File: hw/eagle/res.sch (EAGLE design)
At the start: 63 parts, among them IC2 7805T, IC3 L272M, IC4 L272M, X5 22-23-2021

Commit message: +c
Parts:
- added C16: (no value), rcl:C-EU050-025X075
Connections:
- net +5V: now also C16.1, R4.A; no longer R4.E
- net GND: now also C16.2
- net N$2: now also R4.E; no longer R4.A
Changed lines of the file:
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@@
 <part name="GND35" library="supply1" deviceset="GND" device=""/>
 <part name="GND36" library="supply1" deviceset="GND" device=""/>
+<part name="C16" library="rcl" deviceset="C-EU" device="050-025X075"/>
+<part name="GND37" library="supply1" deviceset="GND" device=""/>
 </parts>
 <sheets>
@@
 <instance part="R2" gate="G$1" x="96.52" y="185.42" rot="R270"/>
 <instance part="R3" gate="G$1" x="152.4" y="177.8" rot="R180"/>
-<instance part="R4" gate="1" x="104.14" y="193.04" rot="MR270"/>
+<instance part="R4" gate="1" x="104.14" y="193.04" rot="R270"/>
 <instance part="R5" gate="G$1" x="144.78" y="200.66" rot="R270"/>
 <instance part="R6" gate="G$1" x="142.24" y="195.58" rot="R270"/>
@@
 <instance part="GND35" gate="1" x="391.16" y="111.76" rot="R90"/>
 <instance part="GND36" gate="1" x="391.16" y="109.22" rot="R90"/>
+<instance part="C16" gate="G$1" x="81.28" y="208.28"/>
+<instance part="GND37" gate="1" x="81.28" y="200.66"/>
 </instances>
 <busses>
@@
 <wire x1="124.46" y1="177.8" x2="121.92" y2="177.8" width="0.1524" layer="91"/>
 <junction x="124.46" y="177.8"/>
-<pinref part="R4" gate="1" pin="A"/>
+<pinref part="R4" gate="1" pin="E"/>
 <wire x1="109.22" y1="193.04" x2="124.46" y2="193.04" width="0.1524" layer="91"/>
 </segment>
@@
 <pinref part="LED2" gate="G$1" pin="C"/>
 <pinref part="GND36" gate="1" pin="GND"/>
+</segment>
+<segment>
+<pinref part="C16" gate="G$1" pin="2"/>
+<pinref part="GND37" gate="1" pin="GND"/>
 </segment>
 </net>
@@
 <segment>
 <pinref part="R2" gate="G$1" pin="1"/>
-<wire x1="96.52" y1="213.36" x2="96.52" y2="210.82" width="0.1524" layer="91"/>
 <wire x1="96.52" y1="210.82" x2="96.52" y2="193.04" width="0.1524" layer="91"/>
 <wire x1="96.52" y1="193.04" x2="96.52" y2="190.5" width="0.1524" layer="91"/>
@@
 <wire x1="142.24" y1="210.82" x2="129.54" y2="210.82" width="0.1524" layer="91"/>
 <wire x1="129.54" y1="210.82" x2="96.52" y2="210.82" width="0.1524" layer="91"/>
-<wire x1="96.52" y1="210.82" x2="73.66" y2="210.82" width="0.1524" layer="91"/>
+<wire x1="96.52" y1="210.82" x2="81.28" y2="210.82" width="0.1524" layer="91"/>
+<wire x1="81.28" y1="210.82" x2="73.66" y2="210.82" width="0.1524" layer="91"/>
 <wire x1="73.66" y1="210.82" x2="66.04" y2="210.82" width="0.1524" layer="91"/>
 <wire x1="96.52" y1="213.36" x2="96.52" y2="210.82" width="0.1524" layer="91"/>
@@
 <junction x="66.04" y="210.82"/>
 <junction x="129.54" y="210.82"/>
-<pinref part="R4" gate="1" pin="E"/>
 <wire x1="129.54" y1="175.26" x2="129.54" y2="210.82" width="0.1524" layer="91"/>
-<wire x1="96.52" y1="193.04" x2="99.06" y2="193.04" width="0.1524" layer="91"/>
 <pinref part="X1" gate="-" pin="3"/>
 <wire x1="160.02" y1="190.5" x2="152.4" y2="190.5" width="0.1524" layer="91"/>
@@
 <junction x="73.66" y="210.82"/>
 <junction x="96.52" y="210.82"/>
-<junction x="96.52" y="193.04"/>
 <junction x="152.4" y="220.98"/>
 <junction x="129.54" y="175.26"/>
-</segment>
-<segment>
+<pinref part="R4" gate="1" pin="A"/>
+<wire x1="96.52" y1="193.04" x2="99.06" y2="193.04" width="0.1524" layer="91"/>
+<pinref part="C16" gate="G$1" pin="1"/>
+<junction x="81.28" y="210.82"/>
+</segment>
+<segment>

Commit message: gnd
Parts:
- added C17: (no value), rcl:C-EU050-025X075
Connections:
- net GND: now also C17.2
- net N$36: now also C17.1
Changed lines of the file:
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@@
 <part name="C16" library="rcl" deviceset="C-EU" device="050-025X075"/>
 <part name="GND37" library="supply1" deviceset="GND" device=""/>
+<part name="C17" library="rcl" deviceset="C-EU" device="050-025X075"/>
+<part name="GND38" library="supply1" deviceset="GND" device=""/>
 </parts>
 <sheets>
@@
 <instance part="C16" gate="G$1" x="81.28" y="208.28"/>
 <instance part="GND37" gate="1" x="81.28" y="200.66"/>
+<instance part="C17" gate="G$1" x="373.38" y="162.56" rot="R90"/>
+<instance part="GND38" gate="1" x="381" y="162.56" rot="R90"/>
 </instances>
 <busses>
@@
 <pinref part="GND37" gate="1" pin="GND"/>
 </segment>
+<segment>
+<pinref part="C17" gate="G$1" pin="2"/>
+<pinref part="GND38" gate="1" pin="GND"/>
+</segment>
 </net>
 <net name="N$8" class="0">
@@
 <junction x="322.58" y="167.64"/>
 <junction x="340.36" y="162.56"/>
+<pinref part="C17" gate="G$1" pin="1"/>
+<junction x="370.84" y="162.56"/>
 </segment>
 </net>
@@
 <pinref part="C16" gate="G$1" pin="1"/>
 <junction x="81.28" y="210.82"/>
-</segment>
-<segment>
+<junction x="96.52" y="193.04"/>
+</segment>
+<segment>

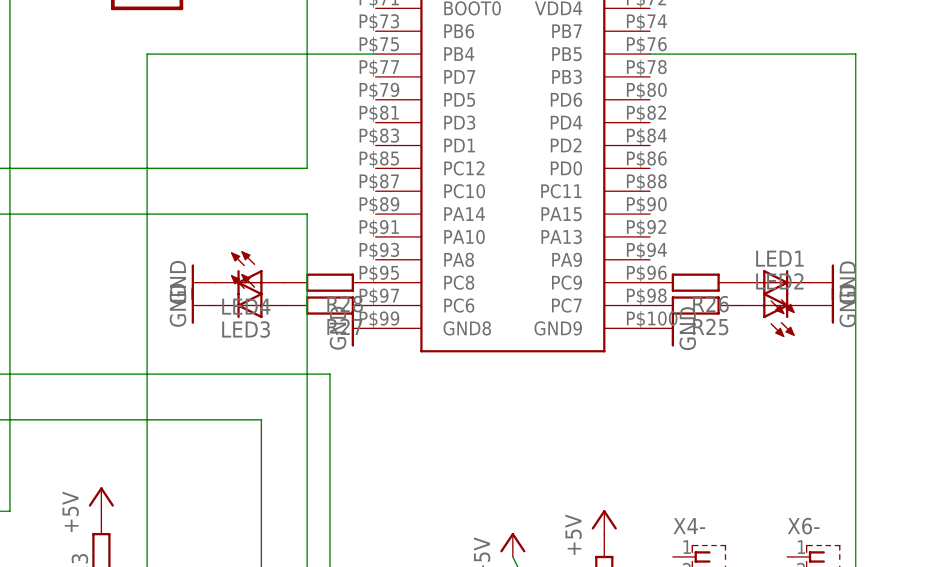
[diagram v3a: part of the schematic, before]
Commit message: led umgeklemmt
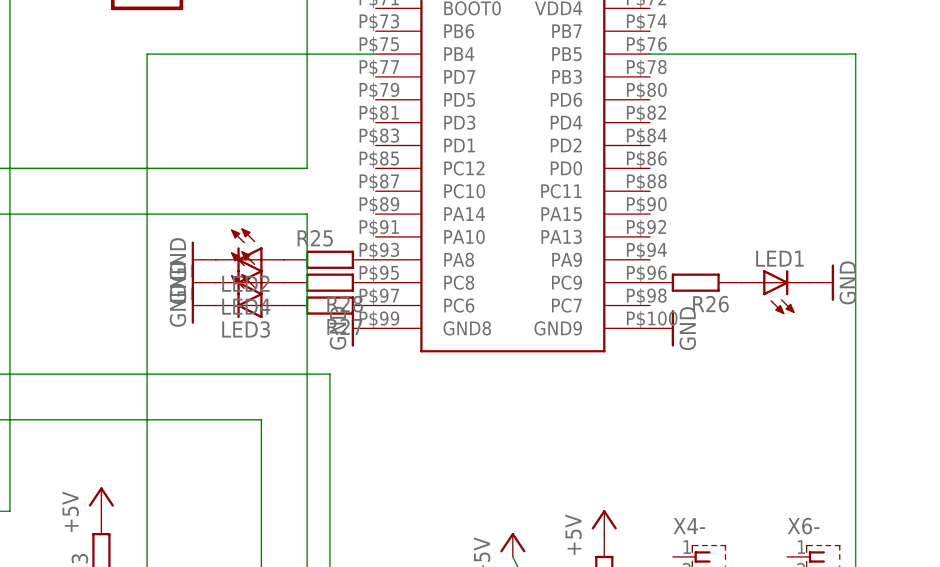
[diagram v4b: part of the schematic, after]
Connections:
- removed net N$46 (its old number): R25.2, U$1.PC7
- new net N$51: R25.2, U$1.PA8
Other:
- moved on the sheet: LED2, R25
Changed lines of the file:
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@@
 <instance part="X6" gate="SHIELD@3" x="395.224" y="64.77"/>
 <instance part="X6" gate="SHIELD@4" x="398.78" y="64.77"/>
-<instance part="R25" gate="G$1" x="375.92" y="109.22" rot="R180"/>
+<instance part="R25" gate="G$1" x="335.28" y="114.3"/>
 <instance part="R26" gate="G$1" x="375.92" y="111.76" rot="R180"/>
 <instance part="R27" gate="G$1" x="335.28" y="109.22" rot="R180"/>
 <instance part="R28" gate="G$1" x="335.28" y="111.76" rot="R180"/>
 <instance part="LED1" gate="G$1" x="383.54" y="111.76" rot="R90"/>
-<instance part="LED2" gate="G$1" x="383.54" y="109.22" rot="R90"/>
+<instance part="LED2" gate="G$1" x="327.66" y="114.3" rot="R270"/>
 <instance part="LED3" gate="G$1" x="327.66" y="109.22" rot="R270"/>
 <instance part="LED4" gate="G$1" x="327.66" y="111.76" rot="R270"/>
@@
 <instance part="GND34" gate="1" x="320.04" y="109.22" rot="R270"/>
 <instance part="GND35" gate="1" x="391.16" y="111.76" rot="R90"/>
-<instance part="GND36" gate="1" x="391.16" y="109.22" rot="R90"/>
+<instance part="GND36" gate="1" x="320.04" y="114.3" rot="R270"/>
 <instance part="C16" gate="G$1" x="81.28" y="208.28"/>
 <instance part="GND37" gate="1" x="81.28" y="200.66"/>
@@
 </segment>
 </net>
-<net name="N$46" class="0">
-<segment>
-<pinref part="U$1" gate="G$1" pin="PC7"/>
-<pinref part="R25" gate="G$1" pin="2"/>
-</segment>
-</net>
 <net name="N$47" class="0">
 <segment>
@@
 </segment>
 </net>
-<net name="N$51" class="0">
+<net name="N$52" class="0">
+<segment>
+<pinref part="R27" gate="G$1" pin="2"/>
+<pinref part="LED3" gate="G$1" pin="A"/>
+</segment>
+</net>
+<net name="N$53" class="0">
+<segment>
+<pinref part="R28" gate="G$1" pin="2"/>
+<pinref part="LED4" gate="G$1" pin="A"/>
+</segment>
+</net>
+<net name="N$46" class="0">
 <segment>
 <pinref part="R25" gate="G$1" pin="1"/>
@@
 </segment>
 </net>
-<net name="N$52" class="0">
-<segment>
-<pinref part="R27" gate="G$1" pin="2"/>
-<pinref part="LED3" gate="G$1" pin="A"/>
-</segment>
-</net>
-<net name="N$53" class="0">
-<segment>
-<pinref part="R28" gate="G$1" pin="2"/>
-<pinref part="LED4" gate="G$1" pin="A"/>
-</segment>
-</net>
+<net name="N$51" class="0">
+<segment>
+<pinref part="U$1" gate="G$1" pin="PA8"/>
+<pinref part="R25" gate="G$1" pin="2"/>
+</segment>
+</net>

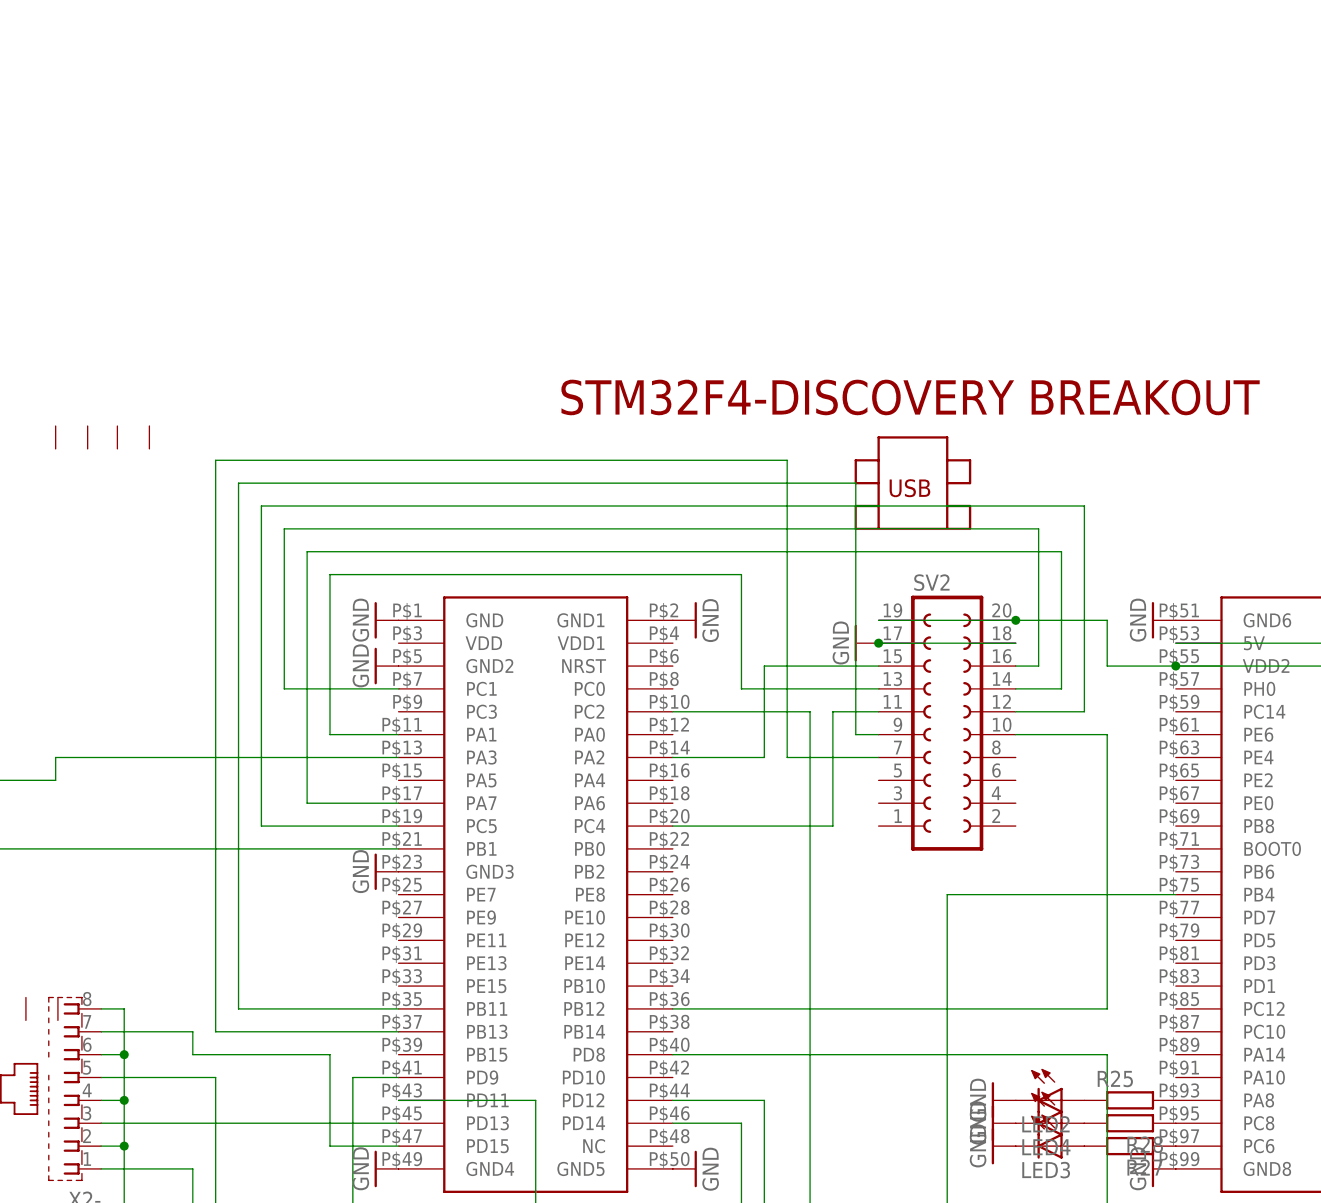
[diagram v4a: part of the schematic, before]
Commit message: schaltplan aufgeräumt
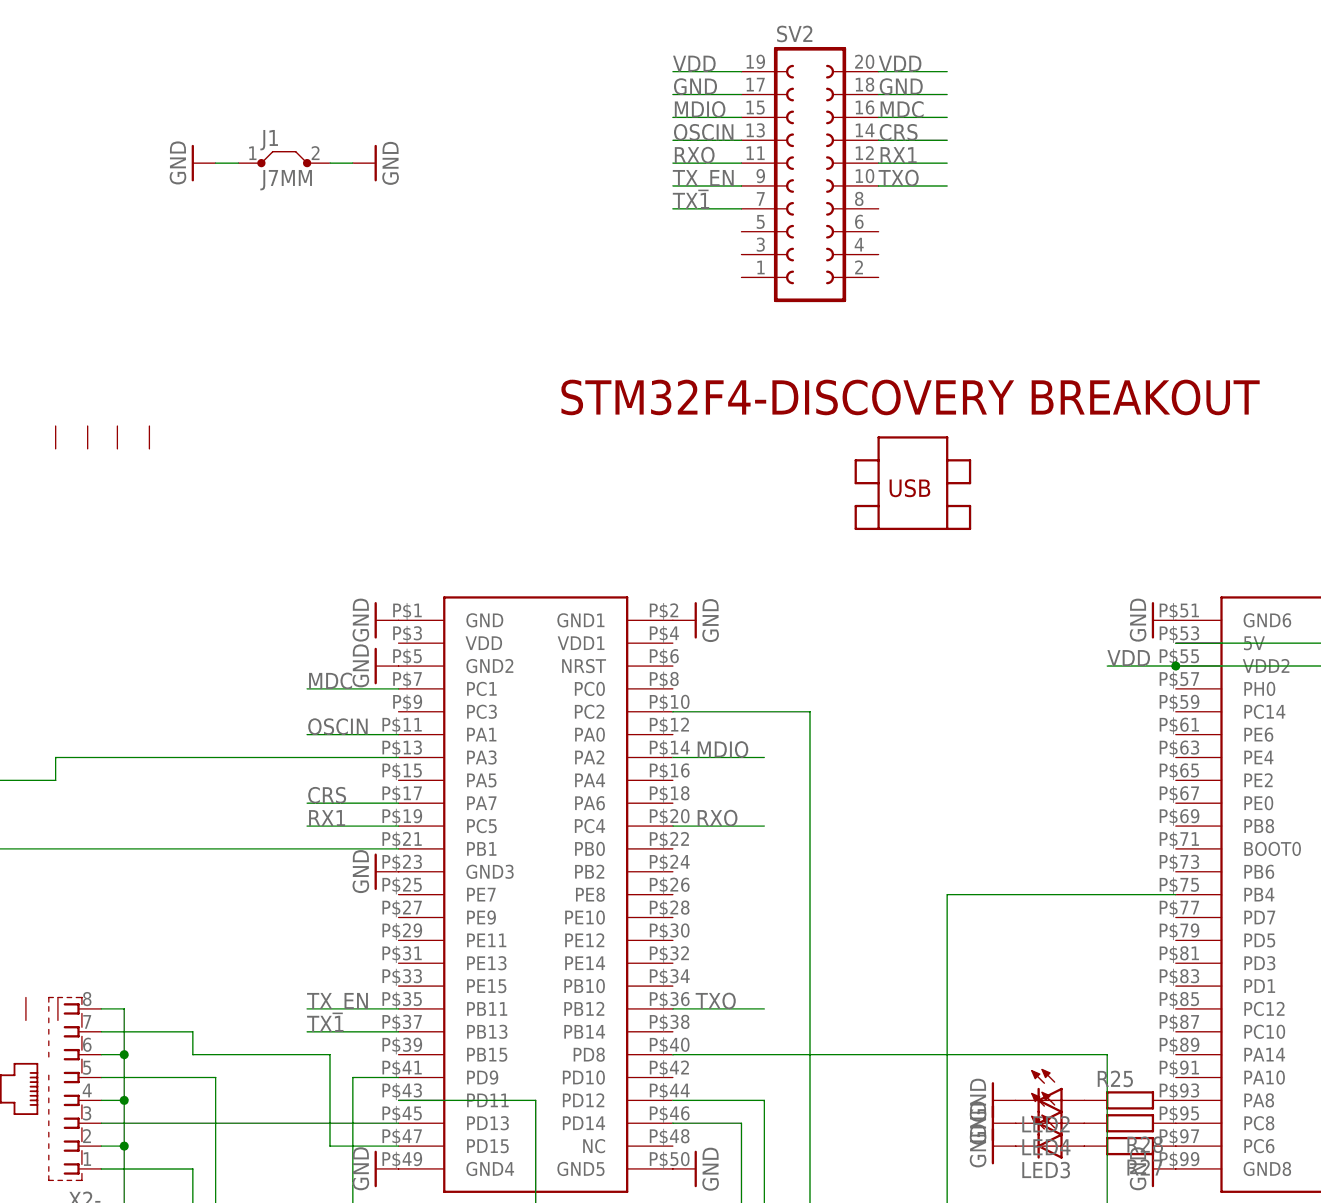
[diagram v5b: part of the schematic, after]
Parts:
- added J1: J7MM, jumper:J7MM
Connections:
- net N$21 renamed TX1
- net N$28 renamed MDIO
- net N$29 renamed OSCIN
- net N$30 renamed CRS
- net N$31 renamed MDC
- net N$32 renamed RXO
- net N$33 renamed RX1
- net N$34 renamed TX_EN
- net N$35 renamed TXO
- net N$36 renamed VDD
- net GND: now also J1.1, J1.2
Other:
- moved on the sheet: SV2

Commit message: vias, pads, ...
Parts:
- removed J1: J7MM, jumper:J7MM
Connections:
- net GND: no longer J1.1, J1.2
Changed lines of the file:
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@@
 <part name="C17" library="rcl" deviceset="C-EU" device="050-025X075"/>
 <part name="GND38" library="supply1" deviceset="GND" device=""/>
-<part name="J1" library="jumper" deviceset="J" device="7MM"/>
-<part name="GND24" library="supply1" deviceset="GND" device=""/>
-<part name="GND39" library="supply1" deviceset="GND" device=""/>
 </parts>
 <sheets>
@@
 <instance part="C17" gate="G$1" x="373.38" y="162.56" rot="R90"/>
 <instance part="GND38" gate="1" x="381" y="162.56" rot="R90"/>
-<instance part="J1" gate="1" x="241.3" y="218.44"/>
-<instance part="GND24" gate="1" x="251.46" y="218.44" rot="R90"/>
-<instance part="GND39" gate="1" x="231.14" y="218.44" rot="R270"/>
 </instances>
 <busses>
@@
 <label x="307.34" y="226.06" size="1.778" layer="95"/>
 </segment>
-<segment>
-<pinref part="GND39" gate="1" pin="GND"/>
-<pinref part="J1" gate="1" pin="1"/>
-<wire x1="233.68" y1="218.44" x2="236.22" y2="218.44" width="0.1524" layer="91"/>
-</segment>
-<segment>
-<pinref part="GND24" gate="1" pin="GND"/>
-<pinref part="J1" gate="1" pin="2"/>
-<wire x1="248.92" y1="218.44" x2="246.38" y2="218.44" width="0.1524" layer="91"/>
-</segment>
 </net>

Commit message: res fehler
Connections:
- removed net N$38: IC4B.+IN, R15.A
- removed net N$39: IC4A.+IN, R16.E
- new net N$21: IC4B.+IN, R15.S
- new net N$28: IC4A.+IN, R16.S
- net +5V: now also R15.A, R16.E; no longer R15.S, R16.S
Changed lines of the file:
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@@
 <part name="GND28" library="supply1" deviceset="GND" device=""/>
 <part name="R15" library="pot" deviceset="TRIM_EU-" device="CA6V"/>
-<part name="P+13" library="supply1" deviceset="+5V" device=""/>
-<part name="P+14" library="supply1" deviceset="+5V" device=""/>
 <part name="R8" library="resistor" deviceset="R-EU_" device="0204/7"/>
 <part name="R17" library="resistor" deviceset="R-EU_" device="0204/7"/>
@@
 <part name="C17" library="rcl" deviceset="C-EU" device="050-025X075"/>
 <part name="GND38" library="supply1" deviceset="GND" device=""/>
+<part name="P+13" library="supply1" deviceset="+5V" device=""/>
+<part name="P+18" library="supply1" deviceset="+5V" device=""/>
 </parts>
 <sheets>
@@
 <instance part="GND28" gate="1" x="160.02" y="175.26"/>
 <instance part="R15" gate="1" x="144.78" y="170.18"/>
-<instance part="P+13" gate="1" x="152.4" y="170.18" rot="R270"/>
-<instance part="P+14" gate="1" x="149.86" y="147.32" rot="R270"/>
 <instance part="R8" gate="G$1" x="134.62" y="160.02" rot="R270"/>
 <instance part="R17" gate="G$1" x="134.62" y="170.18" rot="R270"/>
@@
 <instance part="C17" gate="G$1" x="373.38" y="162.56" rot="R90"/>
 <instance part="GND38" gate="1" x="381" y="162.56" rot="R90"/>
+<instance part="P+13" gate="1" x="144.78" y="162.56" rot="R180"/>
+<instance part="P+18" gate="1" x="142.24" y="139.7" rot="R180"/>
 </instances>
 <busses>
@@
 </segment>
 <segment>
-<pinref part="R15" gate="1" pin="S"/>
-<pinref part="P+13" gate="1" pin="+5V"/>
-</segment>
-<segment>
-<pinref part="P+14" gate="1" pin="+5V"/>
-<pinref part="R16" gate="1" pin="S"/>
-</segment>
-<segment>
 <pinref part="ADM485" gate="G$1" pin="8"/>
 <pinref part="P+16" gate="1" pin="+5V"/>
@@
 <pinref part="R21" gate="G$1" pin="2"/>
 <pinref part="P+17" gate="1" pin="+5V"/>
+</segment>
+<segment>
+<pinref part="R15" gate="1" pin="A"/>
+<pinref part="P+13" gate="1" pin="+5V"/>
+</segment>
+<segment>
+<pinref part="R16" gate="1" pin="E"/>
+<pinref part="P+18" gate="1" pin="+5V"/>
 </segment>
 </net>
@@
 <wire x1="160.02" y1="180.34" x2="190.5" y2="180.34" width="0.1524" layer="91"/>
 <junction x="190.5" y="187.96"/>
-</segment>
-</net>
-<net name="N$38" class="0">
-<segment>
-<pinref part="IC4" gate="B" pin="+IN"/>
-<pinref part="R15" gate="1" pin="A"/>
-<wire x1="144.78" y1="165.1" x2="144.78" y2="162.56" width="0.1524" layer="91"/>
-<wire x1="144.78" y1="162.56" x2="152.4" y2="162.56" width="0.1524" layer="91"/>
-</segment>
-</net>
-<net name="N$39" class="0">
-<segment>
-<pinref part="IC4" gate="A" pin="+IN"/>
-<wire x1="142.24" y1="142.24" x2="152.4" y2="142.24" width="0.1524" layer="91"/>
-<pinref part="R16" gate="1" pin="E"/>
 </segment>
 </net>
@@
 </segment>
 </net>
+<net name="N$21" class="0">
+<segment>
+<pinref part="R15" gate="1" pin="S"/>
+<pinref part="IC4" gate="B" pin="+IN"/>
+<wire x1="149.86" y1="170.18" x2="152.4" y2="170.18" width="0.1524" layer="91"/>
+<wire x1="152.4" y1="170.18" x2="152.4" y2="162.56" width="0.1524" layer="91"/>
+</segment>
+</net>
+<net name="N$28" class="0">
+<segment>
+<pinref part="R16" gate="1" pin="S"/>
+<pinref part="IC4" gate="A" pin="+IN"/>
+<wire x1="147.32" y1="147.32" x2="152.4" y2="147.32" width="0.1524" layer="91"/>
+<wire x1="152.4" y1="147.32" x2="152.4" y2="142.24" width="0.1524" layer="91"/>
+</segment>
+</net>
